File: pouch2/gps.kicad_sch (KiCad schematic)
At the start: 4 parts

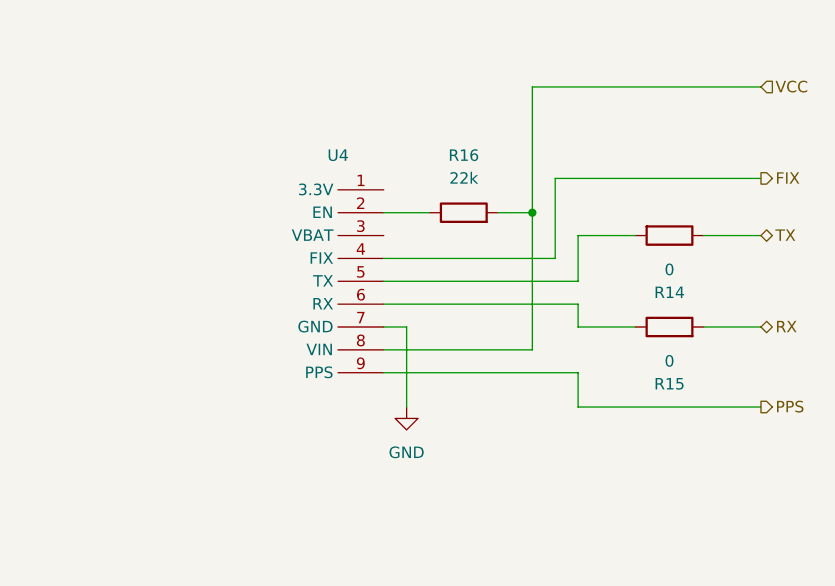
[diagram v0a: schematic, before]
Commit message: added power, sdcard
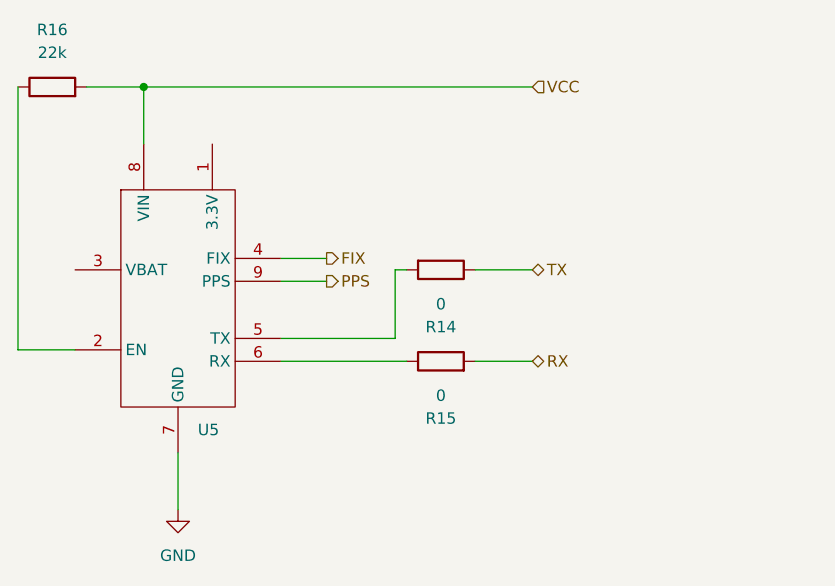
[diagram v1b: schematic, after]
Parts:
- removed U4: ~, symbol SensorBoards:DEBO_GPS
- added U5: ~, symbol SensorBoards:DEBO_GPS
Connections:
- net FIX: now also U5.4 (FIX)
- net GND: now also U5.7 (GND)
- net PPS: now also U5.9 (PPS)
- net VCC: now also U5.8 (VIN)
- net at R14.2: now also U5.5 (TX)
- net at R16.1: now also U5.2 (EN)
- net at R15.1: now also U5.6 (RX)
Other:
- moved on the sheet: R14, R15, R16

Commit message: added pi zero header
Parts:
- R14, R15, R16: footprint (none) -> Resistor_SMD:R_0815_2038Metric
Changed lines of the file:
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@@
 			)
 		)
-		(property "Footprint" ""
+		(property "Footprint" "Resistor_SMD:R_0815_2038Metric"
 			(at 187.96 65.532 90)
 			(effects
@@
 			)
 		)
-		(property "Footprint" ""
+		(property "Footprint" "Resistor_SMD:R_0815_2038Metric"
 			(at 144.78 48.768 90)
 			(effects
@@
 			)
 		)
-		(property "Footprint" ""
+		(property "Footprint" "Resistor_SMD:R_0815_2038Metric"
 			(at 187.96 79.248 90)
 			(effects

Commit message: started PCB design
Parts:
- R301: renamed from R16; footprint Resistor_SMD:R_0815_2038Metric -> Resistor_SMD:R_0805_2012Metric
- R302: renamed from R14; footprint Resistor_SMD:R_0815_2038Metric -> Resistor_SMD:R_0805_2012Metric
- R303: renamed from R15; footprint Resistor_SMD:R_0815_2038Metric -> Resistor_SMD:R_0805_2012Metric
- U301: renamed from U5; footprint (none) -> Connector_PinHeader_2.54mm:PinHeader_1x09_P2.54mm_Vertical
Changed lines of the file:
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@@
 		(dnp no)
 		(fields_autoplaced yes)
-		(property "Reference" "R14"
+		(property "Reference" "R302"
 			(at 187.96 73.66 90)
 			(effects
@@
 			)
 		)
-		(property "Footprint" "Resistor_SMD:R_0815_2038Metric"
+		(property "Footprint" "Resistor_SMD:R_0805_2012Metric"
 			(at 187.96 65.532 90)
 			(effects
@@
 			(project "pouch2"
 				(path "/278cfa6b-9496-4a22-b425-8abdb96793ef/d0ac005f-caac-4a17-bc1d-5f52781e91da"
-					(reference "R14")
+					(reference "R302")
 					(unit 1)
 				)
@@
 		(dnp no)
 		(fields_autoplaced yes)
-		(property "Reference" "#PWR013"
+		(property "Reference" "#PWR0301"
 			(at 158.75 100.33 0)
 			(effects
@@
 			(project ""
 				(path "/278cfa6b-9496-4a22-b425-8abdb96793ef/d0ac005f-caac-4a17-bc1d-5f52781e91da"
-					(reference "#PWR013")
+					(reference "#PWR0301")
 					(unit 1)
 				)
@@
 		(dnp no)
 		(fields_autoplaced yes)
-		(property "Reference" "R16"
+		(property "Reference" "R301"
 			(at 144.78 40.64 90)
 			(effects
@@
 			)
 		)
-		(property "Footprint" "Resistor_SMD:R_0815_2038Metric"
+		(property "Footprint" "Resistor_SMD:R_0805_2012Metric"
 			(at 144.78 48.768 90)
 			(effects
@@
 			(project ""
 				(path "/278cfa6b-9496-4a22-b425-8abdb96793ef/d0ac005f-caac-4a17-bc1d-5f52781e91da"
-					(reference "R16")
+					(reference "R301")
 					(unit 1)
 				)
@@
 		(dnp no)
 		(fields_autoplaced yes)
-		(property "Reference" "U5"
+		(property "Reference" "U301"
 			(at 160.9441 85.09 0)
 			(effects
@@
 			)
 		)
-		(property "Footprint" ""
+		(property "Footprint" "Connector_PinHeader_2.54mm:PinHeader_1x09_P2.54mm_Vertical"
 			(at 158.75 83.82 0)
 			(effects
@@
 			(project ""
 				(path "/278cfa6b-9496-4a22-b425-8abdb96793ef/d0ac005f-caac-4a17-bc1d-5f52781e91da"
-					(reference "U5")
+					(reference "U301")
 					(unit 1)
 				)
@@
 		(dnp no)
 		(fields_autoplaced yes)
-		(property "Reference" "R15"
+		(property "Reference" "R303"
 			(at 187.96 83.82 90)
 			(effects
@@
 			)
 		)
-		(property "Footprint" "Resistor_SMD:R_0815_2038Metric"
+		(property "Footprint" "Resistor_SMD:R_0805_2012Metric"
 			(at 187.96 79.248 90)
 			(effects
@@
 			(project "pouch2"
 				(path "/278cfa6b-9496-4a22-b425-8abdb96793ef/d0ac005f-caac-4a17-bc1d-5f52781e91da"
-					(reference "R15")
-					(unit 1)
-				)
+					(reference "R303")
+					(unit 1)
+				)

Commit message: updated backside of PCB
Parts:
- U301: footprint Connector_PinHeader_2.54mm:PinHeader_1x09_P2.54mm_Vertical -> SensorBoards:DEBO_GPS
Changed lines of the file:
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@@
 			)
 		)
-		(property "Footprint" "Connector_PinHeader_2.54mm:PinHeader_1x09_P2.54mm_Vertical"
+		(property "Footprint" "SensorBoards:DEBO_GPS"
 			(at 158.75 83.82 0)
 			(effects

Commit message: started routing
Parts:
- added R304, R305: 0, Resistor_SMD:R_0805_2012Metric, symbol Device:R
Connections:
- net FIX: now also R305.2; no longer U301.4 (FIX)
- net PPS: now also R304.2; no longer U301.9 (PPS)
- new net: R304.1, U301.9 (PPS)
- new net: R305.1, U301.4 (FIX)
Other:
- moved on the sheet: R302, R303
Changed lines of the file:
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@@
-	(wire
-		(pts
-			(xy 182.88 67.31) (xy 182.88 74.93)
-		)
-		(stroke
-			(width 0)
-			(type default)
-		)
-	)
 	(wire
 		(pts
@@
 	(wire
 		(pts
+			(xy 184.15 77.47) (xy 170.18 77.47)
+		)
+		(stroke
+			(width 0)
+			(type default)
+		)
+	)
+	(wire
+		(pts
 			(xy 148.59 46.99) (xy 154.94 46.99)
 		)
@@
 	(wire
 		(pts
-			(xy 170.18 77.47) (xy 184.15 77.47)
-		)
-		(stroke
-			(width 0)
-			(type default)
-		)
-	)
-	(wire
-		(pts
-			(xy 170.18 68.58) (xy 175.26 68.58)
+			(xy 184.15 85.09) (xy 186.69 85.09)
+		)
+		(stroke
+			(width 0)
+			(type default)
+		)
+	)
+	(wire
+		(pts
+			(xy 170.18 68.58) (xy 186.69 68.58)
+		)
+		(stroke
+			(width 0)
+			(type default)
+		)
+	)
+	(wire
+		(pts
+			(xy 170.18 58.42) (xy 170.18 66.04)
 		)
 		(stroke
@@
 	(wire
 		(pts
-			(xy 198.12 67.31) (xy 191.77 67.31)
-		)
-		(stroke
-			(width 0)
-			(type default)
-		)
-	)
-	(wire
-		(pts
-			(xy 182.88 67.31) (xy 184.15 67.31)
-		)
-		(stroke
-			(width 0)
-			(type default)
-		)
-	)
-	(wire
-		(pts
-			(xy 170.18 66.04) (xy 175.26 66.04)
-		)
-		(stroke
-			(width 0)
-			(type default)
-		)
-	)
-	(wire
-		(pts
-			(xy 170.18 74.93) (xy 182.88 74.93)
-		)
-		(stroke
-			(width 0)
-			(type default)
-		)
-	)
-	(wire
-		(pts
-			(xy 198.12 77.47) (xy 191.77 77.47)
+			(xy 200.66 74.93) (xy 194.31 74.93)
+		)
+		(stroke
+			(width 0)
+			(type default)
+		)
+	)
+	(wire
+		(pts
+			(xy 194.31 58.42) (xy 200.66 58.42)
+		)
+		(stroke
+			(width 0)
+			(type default)
+		)
+	)
+	(wire
+		(pts
+			(xy 170.18 58.42) (xy 186.69 58.42)
+		)
+		(stroke
+			(width 0)
+			(type default)
+		)
+	)
+	(wire
+		(pts
+			(xy 170.18 74.93) (xy 186.69 74.93)
+		)
+		(stroke
+			(width 0)
+			(type default)
+		)
+	)
+	(wire
+		(pts
+			(xy 194.31 68.58) (xy 200.66 68.58)
+		)
+		(stroke
+			(width 0)
+			(type default)
+		)
+	)
+	(wire
+		(pts
+			(xy 184.15 85.09) (xy 184.15 77.47)
+		)
+		(stroke
+			(width 0)
+			(type default)
+		)
+	)
+	(wire
+		(pts
+			(xy 200.66 85.09) (xy 194.31 85.09)
 		)
 		(stroke
@@
 	(hierarchical_label "FIX"
 		(shape output)
-		(at 175.26 66.04 0)
+		(at 200.66 58.42 0)
 		(fields_autoplaced yes)
 		(effects
@@
 	(hierarchical_label "TX"
 		(shape bidirectional)
-		(at 198.12 67.31 0)
+		(at 200.66 74.93 0)
 		(fields_autoplaced yes)
 		(effects
@@
 	(hierarchical_label "RX"
 		(shape bidirectional)
-		(at 198.12 77.47 0)
+		(at 200.66 85.09 0)
 		(fields_autoplaced yes)
 		(effects
@@
 	(hierarchical_label "PPS"
 		(shape output)
-		(at 175.26 68.58 0)
+		(at 200.66 68.58 0)
 		(fields_autoplaced yes)
 		(effects
@@
 	(symbol
 		(lib_id "Device:R")
-		(at 187.96 67.31 270)
+		(at 190.5 74.93 270)
 		(unit 1)
 		(exclude_from_sim no)
@@
 		(fields_autoplaced yes)
 		(property "Reference" "R302"
-			(at 187.96 73.66 90)
+			(at 190.5 81.28 90)
 			(effects
 				(font
@@
 		)
 		(property "Value" "0"
-			(at 187.96 71.12 90)
+			(at 190.5 78.74 90)
 			(effects
 				(font
@@
 		)
 		(property "Footprint" "Resistor_SMD:R_0805_2012Metric"
-			(at 187.96 65.532 90)
+			(at 190.5 73.152 90)
 			(effects
 				(font
@@
 		)
 		(property "Datasheet" "~"
-			(at 187.96 67.31 0)
+			(at 190.5 74.93 0)
 			(effects
 				(font
@@
 		)
 		(property "Description" "Resistor"
-			(at 187.96 67.31 0)
+			(at 190.5 74.93 0)
 			(effects
 				(font
@@
 				(path "/278cfa6b-9496-4a22-b425-8abdb96793ef/d0ac005f-caac-4a17-bc1d-5f52781e91da"
 					(reference "R301")
+					(unit 1)
+				)
+			)
+		)
+	)
+	(symbol
+		(lib_id "Device:R")
+		(at 190.5 68.58 90)
+		(unit 1)
+		(exclude_from_sim no)
+		(in_bom yes)
+		(on_board yes)
+		(dnp no)
+		(property "Reference" "R304"
+			(at 190.5 64.008 90)
+			(effects
+				(font
+					(size 1.27 1.27)
+				)
+			)
+		)
+		(property "Value" "0"
+			(at 190.754 65.786 90)
+			(effects
+				(font
+					(size 1.27 1.27)
+				)
+			)
+		)
+		(property "Footprint" "Resistor_SMD:R_0805_2012Metric"
+			(at 190.5 70.358 90)
+			(effects
+				(font
+					(size 1.27 1.27)
+				)
+				(hide yes)
+			)
+		)
+		(property "Datasheet" "~"
+			(at 190.5 68.58 0)
+			(effects
+				(font
+					(size 1.27 1.27)
+				)
+				(hide yes)
+			)
+		)
+		(property "Description" "Resistor"
+			(at 190.5 68.58 0)
+			(effects
+				(font
+					(size 1.27 1.27)
+				)
+				(hide yes)
+			)
+		)
+		(pin "1"
+		)
+		(pin "2"
+		)
+		(instances
+			(project ""
+				(path "/278cfa6b-9496-4a22-b425-8abdb96793ef/d0ac005f-caac-4a17-bc1d-5f52781e91da"
+					(reference "R304")
+					(unit 1)
+				)
+			)
+		)
+	)
+	(symbol
+		(lib_id "Device:R")
+		(at 190.5 58.42 90)
+		(unit 1)
+		(exclude_from_sim no)
+		(in_bom yes)
+		(on_board yes)
+		(dnp no)
+		(fields_autoplaced yes)
+		(property "Reference" "R305"
+			(at 190.5 52.07 90)
+			(effects
+				(font
+					(size 1.27 1.27)
+				)
+			)
+		)
+		(property "Value" "0"
+			(at 190.5 54.61 90)
+			(effects
+				(font
+					(size 1.27 1.27)
+				)
+			)
+		)
+		(property "Footprint" "Resistor_SMD:R_0805_2012Metric"
+			(at 190.5 60.198 90)
+			(effects
+				(font
+					(size 1.27 1.27)
+				)
+				(hide yes)
+			)
+		)
+		(property "Datasheet" "~"
+			(at 190.5 58.42 0)
+			(effects
+				(font
+					(size 1.27 1.27)
+				)
+				(hide yes)
+			)
+		)
+		(property "Description" "Resistor"
+			(at 190.5 58.42 0)
+			(effects
+				(font
+					(size 1.27 1.27)
+				)
+				(hide yes)
+			)
+		)
+		(pin "1"
+		)
+		(pin "2"
+		)
+		(instances
+			(project ""
+				(path "/278cfa6b-9496-4a22-b425-8abdb96793ef/d0ac005f-caac-4a17-bc1d-5f52781e91da"
+					(reference "R305")
 					(unit 1)
 				)
@@
 	(symbol
 		(lib_id "Device:R")
-		(at 187.96 77.47 90)
+		(at 190.5 85.09 90)
 		(unit 1)
 		(exclude_from_sim no)
@@
 		(fields_autoplaced yes)
 		(property "Reference" "R303"
-			(at 187.96 83.82 90)
+			(at 190.5 91.44 90)
 			(effects
 				(font
@@
 		)
 		(property "Value" "0"
-			(at 187.96 81.28 90)
+			(at 190.5 88.9 90)
 			(effects
 				(font
@@
 		)
 		(property "Footprint" "Resistor_SMD:R_0805_2012Metric"
-			(at 187.96 79.248 90)
+			(at 190.5 86.868 90)
 			(effects
 				(font
@@
 		)
 		(property "Datasheet" "~"
-			(at 187.96 77.47 0)
+			(at 190.5 85.09 0)
 			(effects
 				(font
@@
 		)
 		(property "Description" "Resistor"
-			(at 187.96 77.47 0)
-			(effects
-				(font
+			(at 190.5 85.09 0)
+			(effects
+				(font

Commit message: drawed a lot of things
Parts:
- renumbered R305 to R302, R304 to R303, R302 to R304, R303 to R305
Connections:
- no-connect marks 0 -> 2
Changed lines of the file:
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@@
 		(color 0 0 0 0)
 	)
+	(no_connect
+		(at 146.05 67.31)
+	)
+	(no_connect
+		(at 162.56 52.07)
+	)
+	(wire
+		(pts
+			(xy 162.56 52.07) (xy 162.56 53.34)
+		)
+		(stroke
+			(width 0)
+			(type default)
+		)
+	)
 	(wire
 		(pts
@@
 		(pts
 			(xy 158.75 87.63) (xy 158.75 93.98)
+		)
+		(stroke
+			(width 0)
+			(type default)
+		)
+	)
+	(wire
+		(pts
+			(xy 146.05 67.31) (xy 147.32 67.31)
 		)
 		(stroke
@@
 		(dnp no)
 		(fields_autoplaced yes)
-		(property "Reference" "R302"
+		(property "Reference" "R304"
 			(at 190.5 81.28 90)
 			(effects
@@
 			(project "pouch2"
 				(path "/278cfa6b-9496-4a22-b425-8abdb96793ef/d0ac005f-caac-4a17-bc1d-5f52781e91da"
-					(reference "R302")
+					(reference "R304")
 					(unit 1)
 				)
@@
 		(on_board yes)
 		(dnp no)
-		(property "Reference" "R304"
+		(property "Reference" "R303"
 			(at 190.5 64.008 90)
 			(effects
@@
 			(project ""
 				(path "/278cfa6b-9496-4a22-b425-8abdb96793ef/d0ac005f-caac-4a17-bc1d-5f52781e91da"
-					(reference "R304")
+					(reference "R303")
 					(unit 1)
 				)
@@
 		(dnp no)
 		(fields_autoplaced yes)
-		(property "Reference" "R305"
+		(property "Reference" "R302"
 			(at 190.5 52.07 90)
 			(effects
@@
 			(project ""
 				(path "/278cfa6b-9496-4a22-b425-8abdb96793ef/d0ac005f-caac-4a17-bc1d-5f52781e91da"
-					(reference "R305")
+					(reference "R302")
 					(unit 1)
 				)
@@
 		(dnp no)
 		(fields_autoplaced yes)
-		(property "Reference" "R303"
+		(property "Reference" "R305"
 			(at 190.5 91.44 90)
 			(effects
@@
 			(project "pouch2"
 				(path "/278cfa6b-9496-4a22-b425-8abdb96793ef/d0ac005f-caac-4a17-bc1d-5f52781e91da"
-					(reference "R303")
+					(reference "R305")
 					(unit 1)
 				)

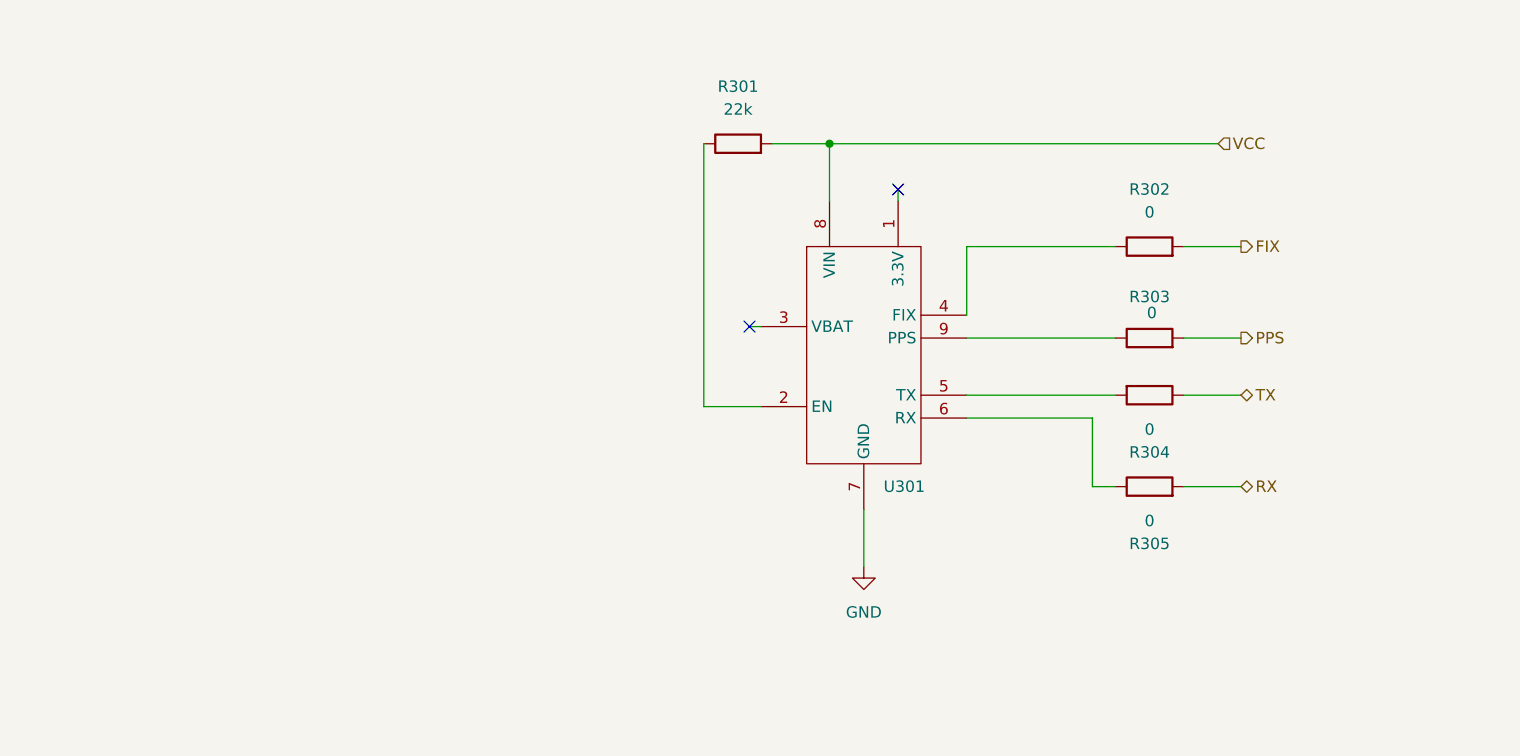
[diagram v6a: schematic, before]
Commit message: updated power routing
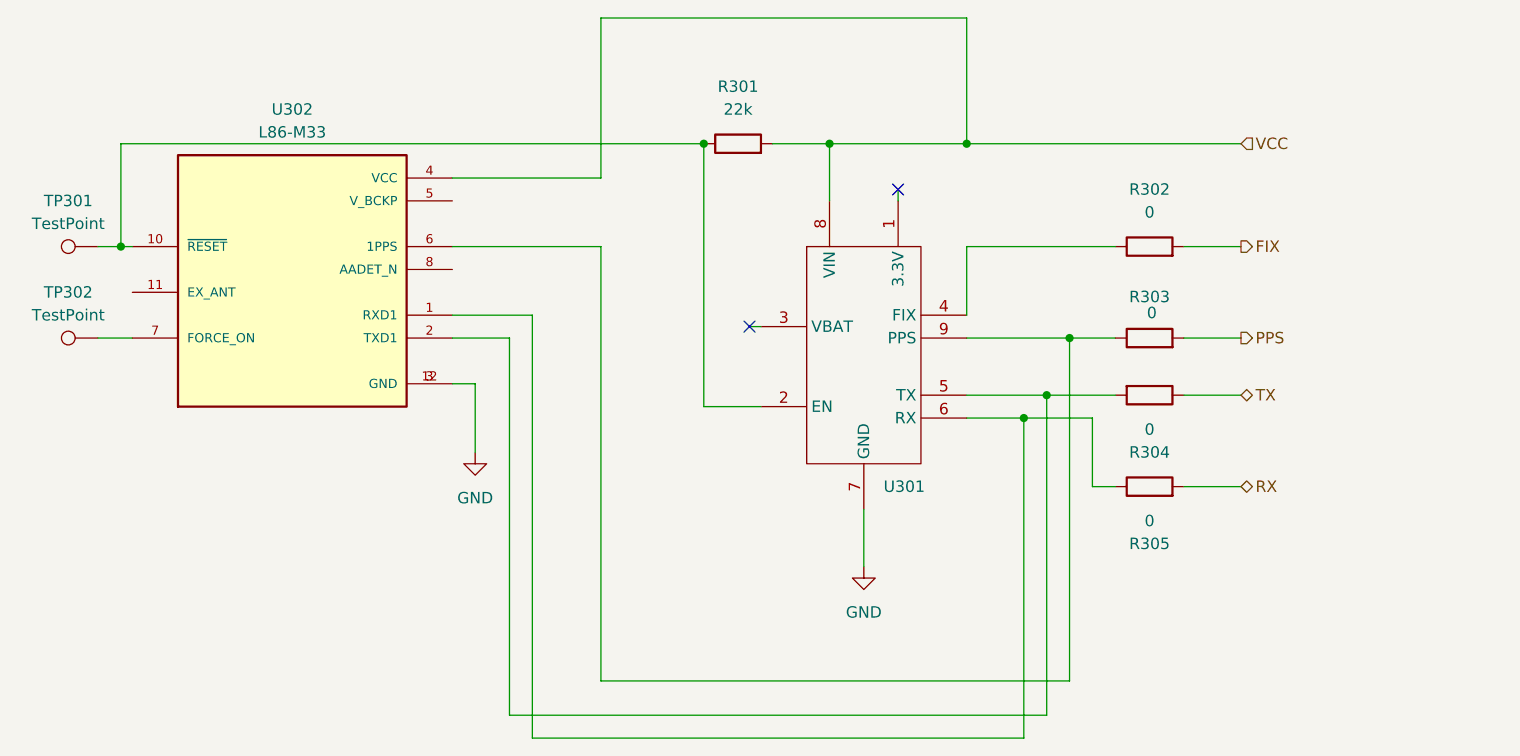
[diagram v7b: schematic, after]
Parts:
- added TP301, TP302: TestPoint, TestPoint:TestPoint_Pad_1.0x1.0mm, symbol Connector:TestPoint
- added U302: L86-M33, L86:XCVR_L86-M33, symbol L86:L86-M33
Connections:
- net GND: now also U302.12 (GND), U302.3 (GND)
- net VCC: now also U302.4 (VCC)
- net at R304.2, U301.5 (TX): now also U302.2 (TXD1)
- net at R301.1, U301.2 (EN): now also TP301.1, U302.10 (~{RESET})
- net at R303.1, U301.9 (PPS): now also U302.6 (1PPS)
- net at R305.1, U301.6 (RX): now also U302.1 (RXD1)
- new net: TP302.1, U302.7 (FORCE_ON)

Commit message: added VCC-battery measurement line
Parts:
- R301: LCSC (none) -> C17560; MPN_Eurocircuit (none) -> GPR080522K
- R302, R303, R304, R305: LCSC (none) -> C17477; MPN_Eurocircuit (none) -> GPR08050R
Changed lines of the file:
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@@
+			)
+		)
+		(property "LCSC" "C17477"
+			(at 190.5 74.93 0)
+			(effects
+				(font
+					(size 1.27 1.27)
+				)
+				(hide yes)
+			)
+		)
+		(property "MPN_Eurocircuit" "GPR08050R"
+			(at 190.5 74.93 0)
+			(effects
+				(font
+					(size 1.27 1.27)
+				)
+				(hide yes)
 			)
 		)
@@
 			)
 		)
+		(property "LCSC" "C17560"
+			(at 144.78 46.99 0)
+			(effects
+				(font
+					(size 1.27 1.27)
+				)
+				(hide yes)
+			)
+		)
+		(property "MPN_Eurocircuit" "GPR080522K"
+			(at 144.78 46.99 0)
+			(effects
+				(font
+					(size 1.27 1.27)
+				)
+				(hide yes)
+			)
+		)
 		(pin "2"
 		)
@@
 			)
 		)
+		(property "MPN_Eurocircuit" ""
+			(at 73.66 58.42 0)
+			(effects
+				(font
+					(size 1.27 1.27)
+				)
+				(hide yes)
+			)
+		)
 		(pin "1"
 		)
@@
 		)
 		(property "Description" "Resistor"
+			(at 190.5 68.58 0)
+			(effects
+				(font
+					(size 1.27 1.27)
+				)
+				(hide yes)
+			)
+		)
+		(property "LCSC" "C17477"
+			(at 190.5 68.58 0)
+			(effects
+				(font
+					(size 1.27 1.27)
+				)
+				(hide yes)
+			)
+		)
+		(property "MPN_Eurocircuit" "GPR08050R"
 			(at 190.5 68.58 0)
 			(effects
@@
 			)
 		)
+		(property "MPN_Eurocircuit" ""
+			(at 73.66 68.58 0)
+			(effects
+				(font
+					(size 1.27 1.27)
+				)
+				(hide yes)
+			)
+		)
 		(pin "1"
 		)
@@
 		)
 		(property "Description" "Resistor"
+			(at 190.5 58.42 0)
+			(effects
+				(font
+					(size 1.27 1.27)
+				)
+				(hide yes)
+			)
+		)
+		(property "LCSC" "C17477"
+			(at 190.5 58.42 0)
+			(effects
+				(font
+					(size 1.27 1.27)
+				)
+				(hide yes)
+			)
+		)
+		(property "MPN_Eurocircuit" "GPR08050R"
 			(at 190.5 58.42 0)
 			(effects
@@
 			)
 		)
+		(property "MPN_Eurocircuit" ""
+			(at 158.75 83.82 0)
+			(effects
+				(font
+					(size 1.27 1.27)
+				)
+				(hide yes)
+			)
+		)
 		(pin "8"
 		)
@@
 			)
 		)
+		(property "MPN_Eurocircuit" ""
+			(at 95.25 60.96 0)
+			(effects
+				(font
+					(size 1.27 1.27)
+				)
+				(hide yes)
+			)
+		)
 		(pin "6"
 		)
@@
 			(at 190.5 85.09 0)
 			(effects
+				(font
+					(size 1.27 1.27)
+				)
+				(hide yes)
+			)
+		)
+		(property "LCSC" "C17477"
+			(at 190.5 85.09 0)
+			(effects
+				(font
+					(size 1.27 1.27)
+				)
+				(hide yes)
+			)
+		)
+		(property "MPN_Eurocircuit" "GPR08050R"
+			(at 190.5 85.09 0)
+			(effects
